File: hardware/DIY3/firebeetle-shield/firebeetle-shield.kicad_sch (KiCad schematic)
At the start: 8 parts, among them J1 Conn_01x14_Female, J2 Conn_01x06_Female (DS3231), J3 Conn_01x04_Male (MS5803), J4 Conn_01x06_Female (microSD), J5 Conn_01x18_Female

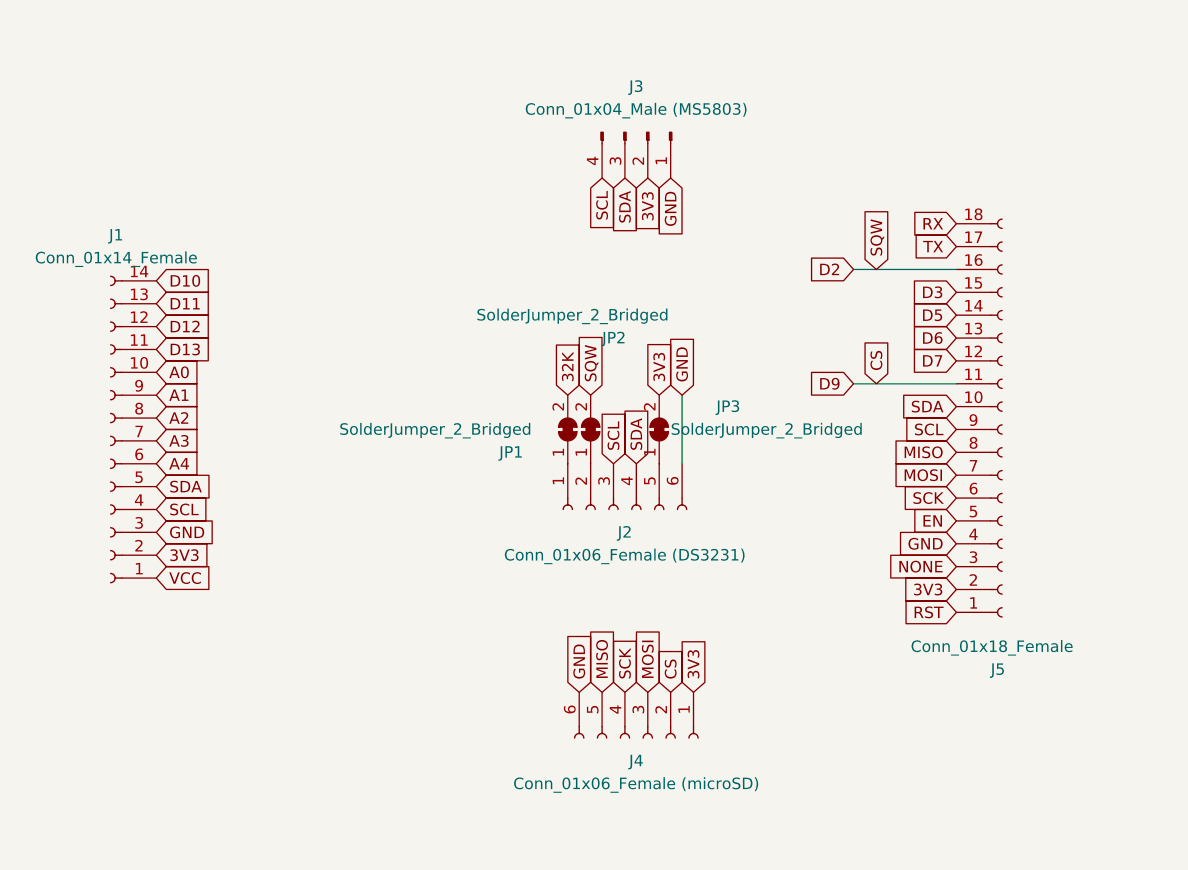
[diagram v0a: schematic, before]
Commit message: Fix schematic errors/conflicts and clean up
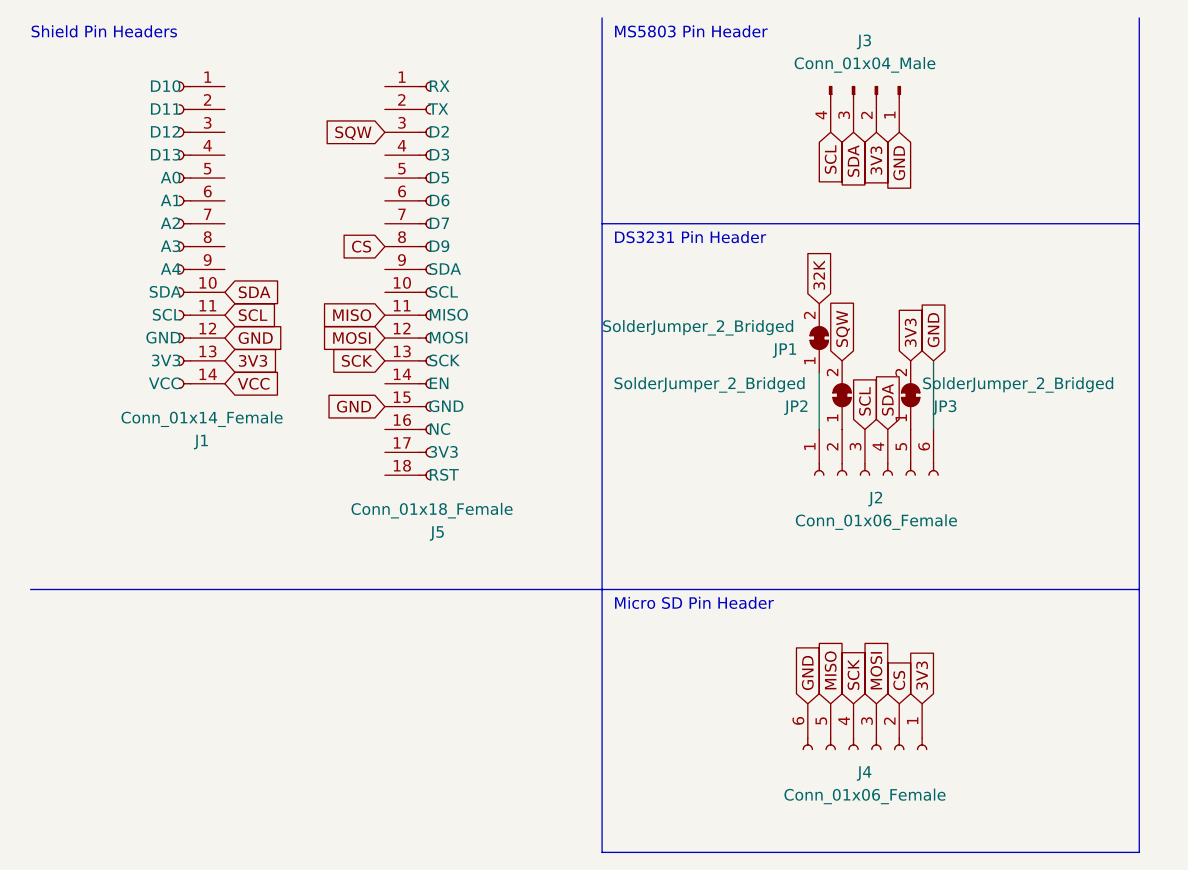
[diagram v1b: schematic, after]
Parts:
- J2: value Conn_01x06_Female (DS3231) -> Conn_01x06_Female
- J3: value Conn_01x04_Male (MS5803) -> Conn_01x04_Male
- J4: value Conn_01x06_Female (microSD) -> Conn_01x06_Female
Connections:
- net A0 is gone; now on net SDA: J1.10 (SDA)
- net D10 is gone; now on net VCC: J1.14 (VCC)
- net D11 is gone; now on net 3V3: J1.13 (3V3)
- net D12 is gone; now on net GND: J1.12 (GND)
- net D13 is gone; now on net SCL: J1.11 (SCL)
- net D3 is gone; now on net GND: J5.15 (GND)
- net D6 is gone; now on net SCK: J5.13 (SCK)
- net D7 is gone; now on net MOSI: J5.12 (MOSI)
- net 3V3: no longer J1.2 (Pin_2), J5.2 (Pin_2)
- net CS: now also J5.8 (D9); no longer J5.11 (Pin_11)
- net GND: no longer J1.3 (Pin_3), J5.4 (Pin_4)
- net MISO: now also J5.11 (MISO); no longer J5.8 (Pin_8)
- net MOSI: no longer J5.7 (Pin_7)
- net SCK: no longer J5.6 (Pin_6)
- net SCL: no longer J1.4 (Pin_4), J5.9 (Pin_9)
- net SDA: no longer J1.5 (Pin_5), J5.10 (Pin_10)
- net VCC: no longer J1.1 (Pin_1)
- net A1: no longer names the net of J1.9 (A4)
- net A2: no longer names the net of J1.8 (A3)
- net A3: no longer names the net of J1.7 (A2)
- net A4: no longer names the net of J1.6 (A1)
- net D2: no longer names the net of J5.16 (NC)
- net D2: no longer JP2.2 (B)
- net D5: no longer names the net of J5.14 (EN)
- net EN: no longer names the net of J5.5 (D5)
- net NONE renamed SQW
- net SQW: now also JP2.2 (B)
- net RST: no longer names the net of J5.1 (RX)
- net RX: no longer names the net of J5.18 (RST)
- net TX: no longer names the net of J5.17 (3V3)
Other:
- note added: "DS3231 Pin Header"
- note added: "MS5803 Pin Header"
- note added: "Micro SD Pin Header"
- note added: "Shield Pin Headers"
- moved on the sheet: J2, J3, J4, JP1, JP2, JP3
